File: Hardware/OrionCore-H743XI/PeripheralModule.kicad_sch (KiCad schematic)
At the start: 1 part, among them J1 FANKE_RGB888

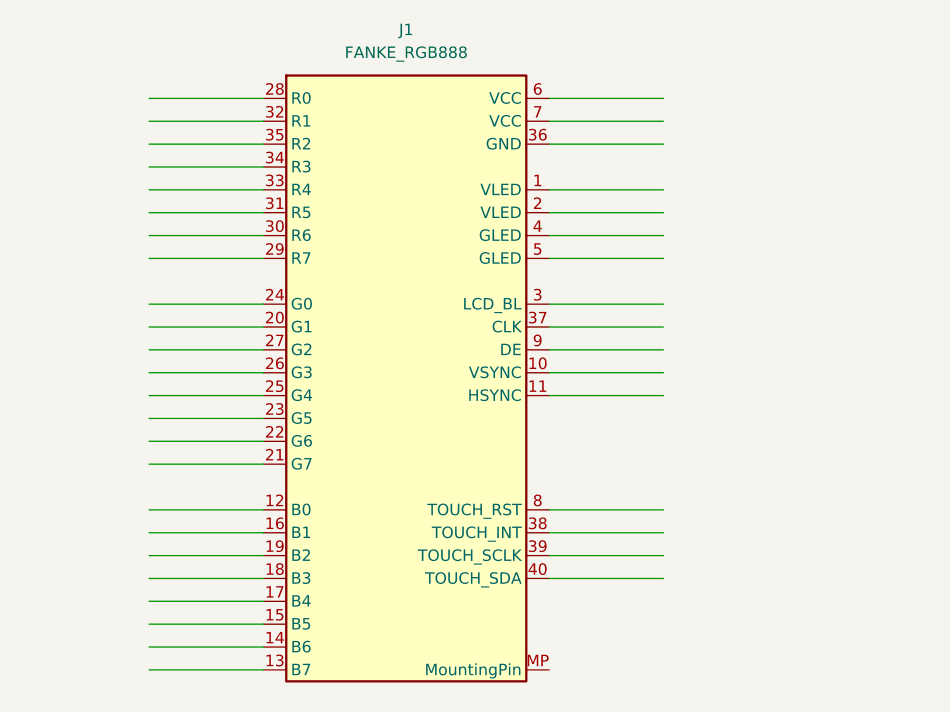
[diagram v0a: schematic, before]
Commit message: Update SDRAM, RGB LCD, QSPI Flash Pin
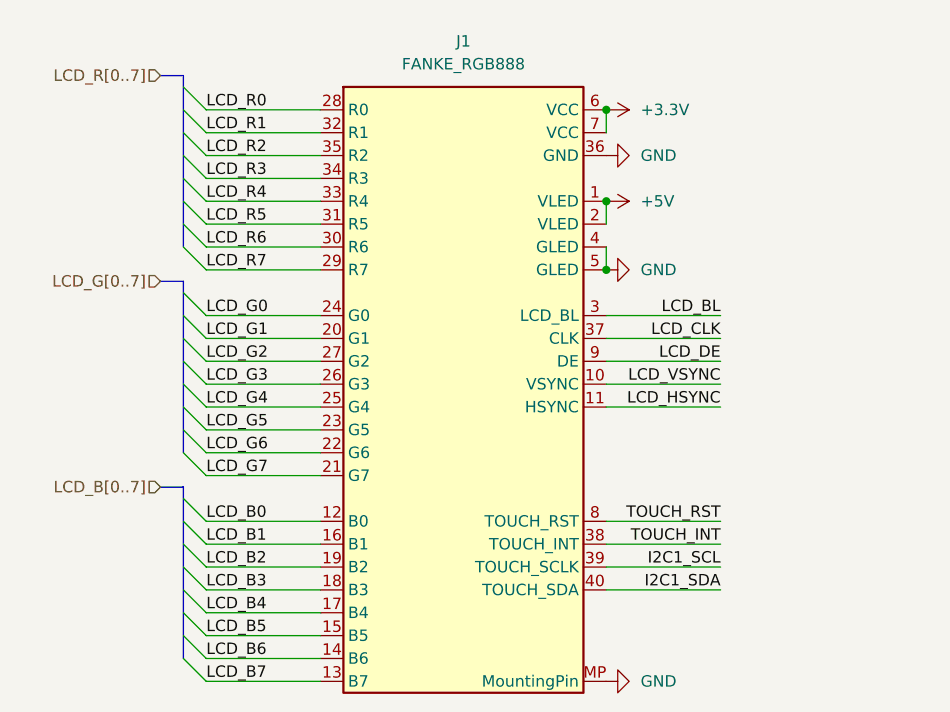
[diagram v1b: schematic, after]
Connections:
- net +5V: now reaches J1.1 (VLED)
- net +5V: now also J1.2 (VLED)
- net LCD_VSYNC: now reaches J1.10 (VSYNC)
- net LCD_HSYNC: now reaches J1.11 (HSYNC)
- net LCD_B0: now reaches J1.12 (B0)
- net LCD_B7: now reaches J1.13 (B7)
- net LCD_B6: now reaches J1.14 (B6)
- net LCD_B5: now reaches J1.15 (B5)
- net LCD_B1: now reaches J1.16 (B1)
- net LCD_B4: now reaches J1.17 (B4)
- net LCD_B3: now reaches J1.18 (B3)
- net LCD_B2: now reaches J1.19 (B2)
- net LCD_G1: now reaches J1.20 (G1)
- net LCD_G7: now reaches J1.21 (G7)
- net LCD_G6: now reaches J1.22 (G6)
- net LCD_G5: now reaches J1.23 (G5)
- net LCD_G0: now reaches J1.24 (G0)
- net LCD_G4: now reaches J1.25 (G4)
- net LCD_G3: now reaches J1.26 (G3)
- net LCD_G2: now reaches J1.27 (G2)
- net LCD_R0: now reaches J1.28 (R0)
- net LCD_R7: now reaches J1.29 (R7)
- net LCD_BL: now reaches J1.3 (LCD_BL)
- net LCD_R6: now reaches J1.30 (R6)
- net LCD_R5: now reaches J1.31 (R5)
- net LCD_R1: now reaches J1.32 (R1)
- net LCD_R4: now reaches J1.33 (R4)
- net LCD_R3: now reaches J1.34 (R3)
- net LCD_R2: now reaches J1.35 (R2)
- net GND: now reaches J1.36 (GND)
- net GND: now also J1.4 (GLED), J1.5 (GLED), J1.MP (MountingPin)
- net LCD_CLK: now reaches J1.37 (CLK)
- net TOUCH_INT: now reaches J1.38 (TOUCH_INT)
- net I2C1_SCL: now reaches J1.39 (TOUCH_SCLK)
- net I2C1_SDA: now reaches J1.40 (TOUCH_SDA)
- net +3.3V: now reaches J1.6 (VCC)
- net +3.3V: now also J1.7 (VCC)
- net TOUCH_RST: now reaches J1.8 (TOUCH_RST)
- net LCD_DE: now reaches J1.9 (DE)
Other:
- moved on the sheet: J1

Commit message: feat: update dual qspi
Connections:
- net I2C1_SCL renamed I2C1.SCL
- net I2C1_SDA renamed I2C1.SDA
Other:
- company: (none) -> Peakors
- title: (none) -> OrionCore
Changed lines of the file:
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@@
 	(generator_version "10.0")
 	(paper "A4")
+	(title_block
+		(title "OrionCore")
+		(date "2026-05-15")
+		(rev "V1.0")
+		(company "Peakors")
+	)
 	(junction
 		(at 87.63 45.72)
@@
 	)
 	(bus_entry
+		(at 100.33 88.9)
+		(size 2.54 2.54)
+		(stroke
+			(width 0)
+			(type default)
+		)
+	)
+	(bus_entry
 		(at 43.18 48.26)
 		(size -2.54 -2.54)
@@
 	)
 	(bus_entry
+		(at 100.33 86.36)
+		(size 2.54 2.54)
+		(stroke
+			(width 0)
+			(type default)
+		)
+	)
+	(bus_entry
 		(at 43.18 93.98)
 		(size -2.54 -2.54)
@@
 		)
 	)
+	(bus
+		(pts
+			(xy 102.87 88.9) (xy 102.87 92.71)
+		)
+		(stroke
+			(width 0)
+			(type default)
+		)
+	)
 	(wire
 		(pts
@@
 		)
 	)
+	(bus
+		(pts
+			(xy 102.87 92.71) (xy 105.41 92.71)
+		)
+		(stroke
+			(width 0)
+			(type default)
+		)
+	)
 	(wire
 		(pts
@@
 		)
 	)
-	(label "I2C1_SCL"
+	(label "I2C1.SCL"
 		(at 100.33 86.36 180)
 		(effects
@@
 		)
 	)
-	(label "I2C1_SDA"
+	(label "I2C1.SDA"
 		(at 100.33 88.9 180)
 		(effects
@@
 		)
 	)
+	(hierarchical_label "TOUCH_RST"
+		(shape input)
+		(at 100.33 81.28 0)
+		(effects
+			(font
+				(size 1.27 1.27)
+			)
+			(justify left)
+		)
+	)
+	(hierarchical_label "LCD_CLK"
+		(shape input)
+		(at 100.33 60.96 0)
+		(effects
+			(font
+				(size 1.27 1.27)
+			)
+			(justify left)
+		)
+	)
 	(hierarchical_label "LCD_R[0..7]"
 		(shape input)
@@
 		)
 	)
+	(hierarchical_label "I2C1{SCL,SDA}"
+		(shape input)
+		(at 105.41 92.71 0)
+		(effects
+			(font
+				(size 1.27 1.27)
+			)
+			(justify left)
+		)
+	)
+	(hierarchical_label "LCD_VSYNC"
+		(shape input)
+		(at 100.33 66.04 0)
+		(effects
+			(font
+				(size 1.27 1.27)
+			)
+			(justify left)
+		)
+	)
+	(hierarchical_label "LCD_HSYNC"
+		(shape input)
+		(at 100.33 68.58 0)
+		(effects
+			(font
+				(size 1.27 1.27)
+			)
+			(justify left)
+		)
+	)
+	(hierarchical_label "LCD_DE"
+		(shape input)
+		(at 100.33 63.5 0)
+		(effects
+			(font
+				(size 1.27 1.27)
+			)
+			(justify left)
+		)
+	)
+	(hierarchical_label "LCD_BL"
+		(shape input)
+		(at 100.33 58.42 0)
+		(effects
+			(font
+				(size 1.27 1.27)
+			)
+			(justify left)
+		)
+	)
+	(hierarchical_label "TOUCH_INT"
+		(shape input)
+		(at 100.33 83.82 0)
+		(effects
+			(font
+				(size 1.27 1.27)
+			)
+			(justify left)
+		)
+	)
